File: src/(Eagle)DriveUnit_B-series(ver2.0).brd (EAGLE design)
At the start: 65.7 x 51 mm, 70 parts, among them IC1 A3921, IC2 CZ3A07, SW1 TVAF06-A020B-R, SW2 TVAF06-A020B-R, SW3 THAF01-NC-R, SW4 SS-12D00G3

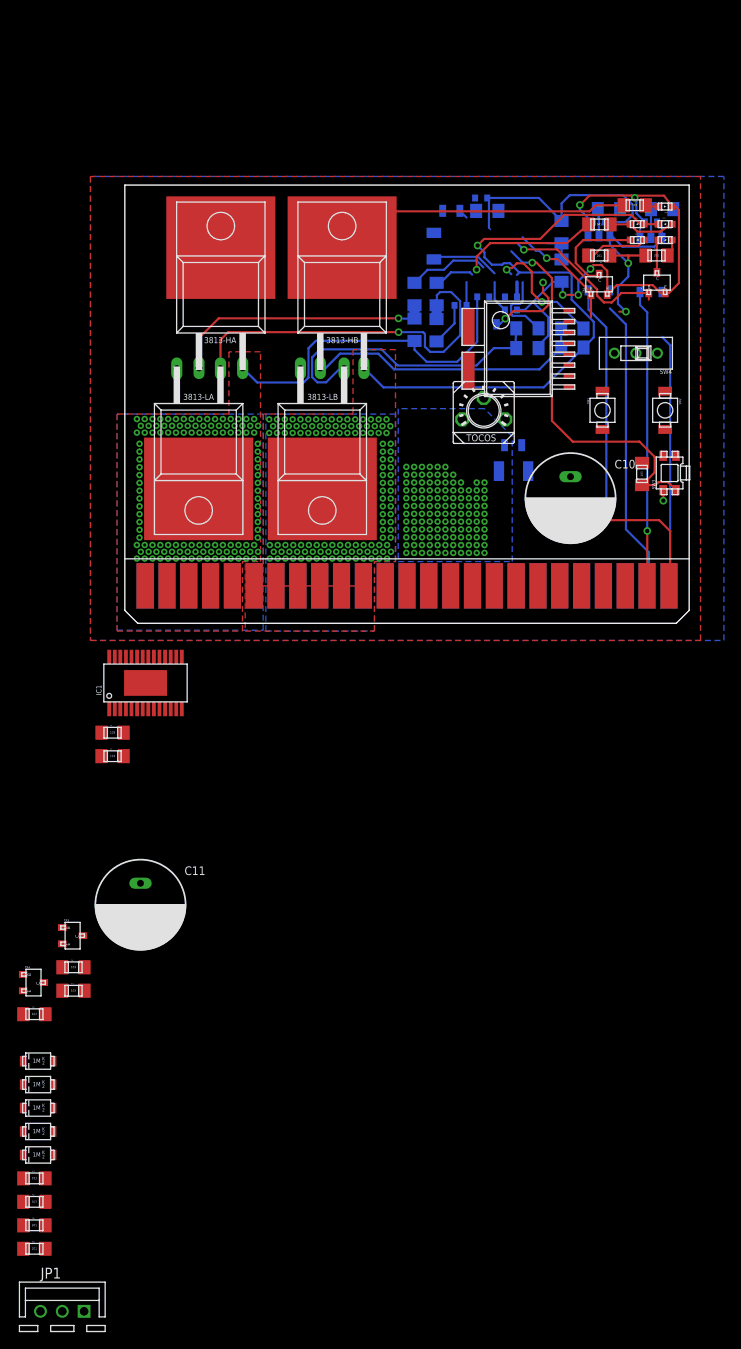
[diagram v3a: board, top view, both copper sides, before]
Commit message: [remove:電流センサを取り除いた
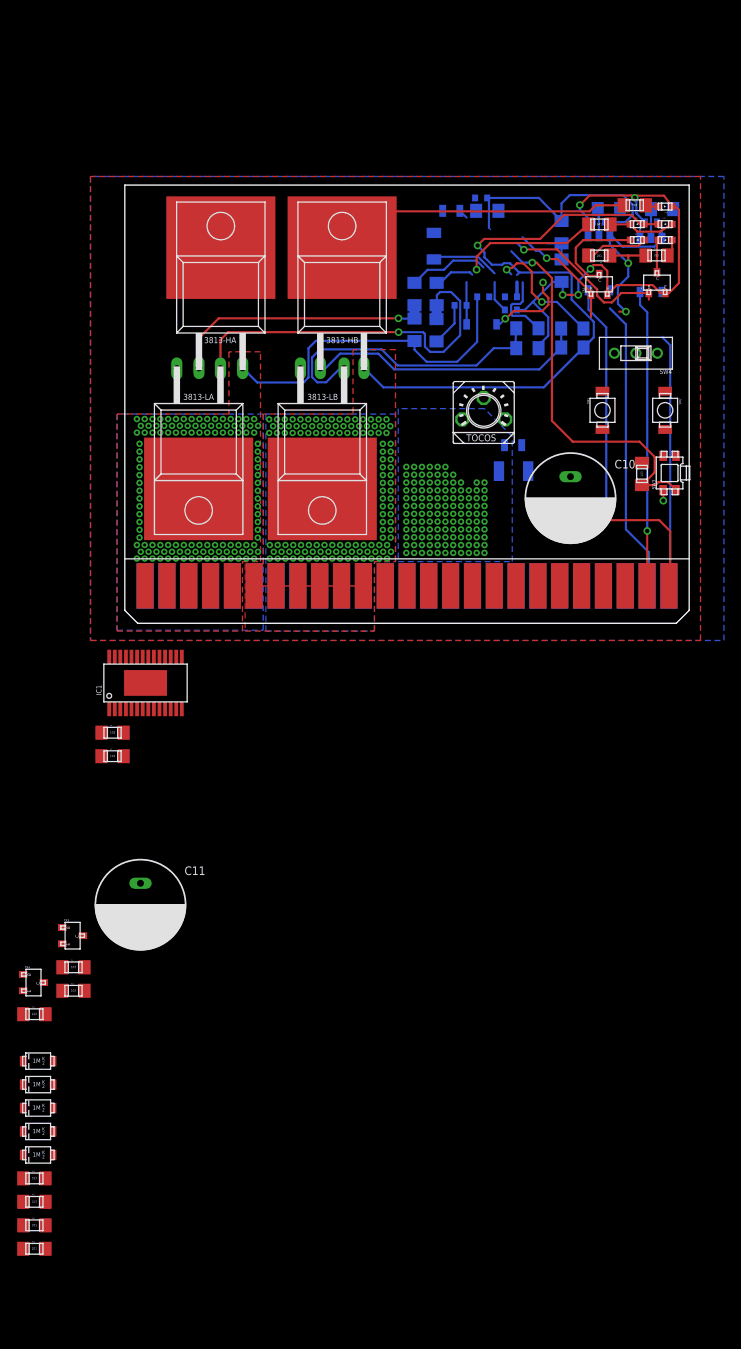
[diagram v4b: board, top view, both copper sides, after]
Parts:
- removed IC2: CZ3A07, CZ3A07:CZ3A07
- removed JP1: (no value), con-jst-xh:B3B-XH
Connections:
- removed net VOUT: JP1.2
- net GND_IN: no longer IC2.OCD2, IC2.REF2, IC2.VSS1, JP1.1
- net SA: no longer IC2.IP
- net SB: no longer IC2.IN
- net VCC_IN: no longer JP1.3
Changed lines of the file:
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@@
 </element>
 <element name="R28" library="GF063P B104K" package="GF063PB104K" value="100k" x="38.22" y="20.93" smashed="yes"/>
-<element name="IC2" library="CZ3A07" package="CZ3A07" value="CZ3A07" x="41.86" y="26.39" smashed="yes"/>
-<element name="JP1" library="con-jst-xh" package="B3B-XH" value="" x="-7.28" y="-80.08" smashed="yes">
-<attribute name="NAME" x="-9.82" y="-76.27" size="1.27" layer="25"/>
-<attribute name="VALUE" x="-9.82" y="-83.89" size="1.27" layer="27"/>
-</element>
 </elements>
 <signals>
@@
 <wire x1="45.63" y1="40.5332875" x2="45.91243125" y2="40.81571875" width="0.254" layer="16"/>
 <contactref element="IC1" pad="4"/>
-<contactref element="IC2" pad="IN"/>
 <wire x1="45.63" y1="40.5332875" x2="45.64" y2="39.71" width="0" layer="19" extent="16-16"/>
 <wire x1="27.72" y1="23.73" x2="27.83" y2="29.72" width="0" layer="19" extent="1-1"/>
@@
 <wire x1="17.6" y1="4.35" x2="17.6" y2="4.35" width="0" layer="19" extent="1-16"/>
 <wire x1="22.98" y1="15.6446" x2="23.17" y2="22.15" width="0" layer="19" extent="1-1"/>
-<wire x1="39.915" y1="29.39" x2="45.64" y2="38" width="0" layer="19" extent="1-16"/>
 <wire x1="0.13" y1="-10" x2="15.06" y2="4.35" width="0" layer="19" extent="1-1"/>
 </signal>
@@
 </polygon>
 <contactref element="IC1" pad="11"/>
-<contactref element="IC2" pad="IP"/>
 <wire x1="41.08" y1="38.07" x2="41.08" y2="41.0132" width="0" layer="19" extent="16-16"/>
-<wire x1="39.915" y1="34.49" x2="41.01" y2="38" width="0" layer="19" extent="1-16"/>
 <wire x1="13.23" y1="23.77" x2="13.71" y2="29.72" width="0" layer="19" extent="1-1"/>
 <wire x1="12.775" y1="22.98" x2="13.23" y2="23.77" width="0" layer="19" extent="1-1"/>
@@
 <wire x1="60.8" y1="4.37" x2="60.78" y2="4.35" width="0.1524" layer="1"/>
 <contactref element="TLP2" pad="3"/>
-<contactref element="JP1" pad="1"/>
-<contactref element="IC2" pad="VSS1"/>
-<contactref element="IC2" pad="REF2"/>
-<contactref element="IC2" pad="OCD2"/>
-<wire x1="51.705" y1="35.115" x2="53.91" y2="38.75" width="0" layer="19" extent="1-16"/>
-<wire x1="51.705" y1="30.035" x2="51.705" y2="35.115" width="0" layer="19" extent="1-1"/>
-<wire x1="51.705" y1="27.495" x2="51.705" y2="30.035" width="0" layer="19" extent="1-1"/>
 <wire x1="59.96" y1="38.55" x2="53.91" y2="38.75" width="0" layer="19" extent="16-16"/>
-<wire x1="-4.74" y1="-80.08" x2="60.78" y2="4.35" width="0" layer="19" extent="1-1"/>
 </signal>
 <signal name="PWM_IN">
@@
 <wire x1="58.32" y1="10.93" x2="61" y2="8.25" width="0.254" layer="16"/>
 <wire x1="61" y1="8.25" x2="61" y2="4.57" width="0.254" layer="16"/>
-<contactref element="JP1" pad="3"/>
-<wire x1="60.78" y1="4.35" x2="-9.82" y2="-80.08" width="0" layer="19" extent="16-16"/>
 </signal>
 <signal name="N$1">
@@
 <wire x1="44.27" y1="23.73" x2="41.77" y2="26.23" width="0" layer="19" extent="1-1"/>
 </signal>
-<signal name="VOUT">
-<contactref element="JP1" pad="2"/>
-</signal>
 </signals>

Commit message: [add]配線の追加
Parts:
- removed 3813-HA, 3813-HB, 3813-LA, 3813-LB: IRLB3813NOHOLE, OKUDA_libraries:TO-220AB-NOHOLE
- added HA, HB, LA, LB: IRLB3813NOHOLE, OKUDA_libraries:TO-220AB-NOHOLE
- moved R25 143.0 mm to (36.0, 67.4), flipped to the bottom
- moved R24 138.7 mm to (30.9, 67.4), flipped to the bottom
- moved D5 129.6 mm to (16.9, 69.9), flipped to the bottom
- moved D4 125.9 mm to (11.9, 69.9), flipped to the bottom
- moved R17 122.5 mm to (51.2, 64.8), flipped to the bottom
- moved R23 119.0 mm to (25.8, 67.4), flipped to the bottom
- moved D6 117.6 mm to (53.1, 39.0), turned to 90 degrees
- moved R6 117.4 mm to (52.5, 61.0), flipped to the bottom
- moved D3 115.7 mm to (55.9, 42.8), turned to 270 degrees
- moved R27 114.3 mm to (63.3, 13.4), flipped to the bottom, turned to 270 degrees
- moved R26 109.5 mm to (59.1, 13.4), flipped to the bottom, turned to 270 degrees
- moved TR4 109.1 mm to (37.3, 54.7), flipped to the bottom
- moved D2 105.3 mm to (51.4, 22.3), turned to 270 degrees
- moved TR3 100.1 mm to (32.2, 54.7), flipped to the bottom
- moved R5 83.8 mm to (61.3, 38.5)
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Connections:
- net GND: now also LA.SOURCE, LB.SOURCE; no longer 3813-LA.SOURCE, 3813-LB.SOURCE
- net N$13: now also HA.GATE; no longer 3813-HA.GATE
- net N$21: now also HB.GATE; no longer 3813-HB.GATE
- net N$25: now also LA.GATE; no longer 3813-LA.GATE
- net N$26: now also LB.GATE; no longer 3813-LB.GATE
- net SA: now also HA.SOURCE, LA.DRAIN; no longer 3813-HA.SOURCE, 3813-LA.DRAIN
- net SB: now also HB.SOURCE, LB.DRAIN; no longer 3813-HB.SOURCE, 3813-LB.DRAIN
- net VCC: now also HA.DRAIN, HB.DRAIN; no longer 3813-HA.DRAIN, 3813-HB.DRAIN
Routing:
- net SB: track 93.0 -> 0.00 mm, vias 123 -> 0
- net GND: track 72.9 -> 3.98 mm, vias 6 -> 0
- net SA: track 56.1 -> 0.00 mm, vias 123 -> 0
- net V5: track 56.9 -> 3.96 mm, vias 2 -> 0
- net VCC: track 46.2 -> 0.00 mm, vias 124 -> 0
- net RESET: track 44.7 -> 0.00 mm, vias 1 -> 0
- net N$25: track 44.3 -> 0.00 mm, vias 1 -> 0
- net PWM_IN: track 42.0 -> 0.00 mm, vias 1 -> 0
- net N$26: track 35.1 -> 0.00 mm
- net GND_IN: track 34.6 -> 0.00 mm, vias 1 -> 0
- net VCC_IN: track 34.3 -> 0.00 mm
- net N$21: track 32.8 -> 0.00 mm
- net N$13: track 31.1 -> 0.00 mm, vias 1 -> 0
- net DIR_IN: track 29.5 -> 0.00 mm
- net FF1: track 19.9 -> 0.00 mm, vias 1 -> 0
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- removed copper zone on layer 1, net SA
- removed copper zone on layer 16, net SA
- removed copper zone on layer 1, net SB
- removed copper zone on layer 16, net SB
- removed copper zone on layer 16, net VCC
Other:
- board text added: "FF1"
- board text added: "FF2"
- board text added: "POW"
- board text added: "SA"
- board text added: "SB"

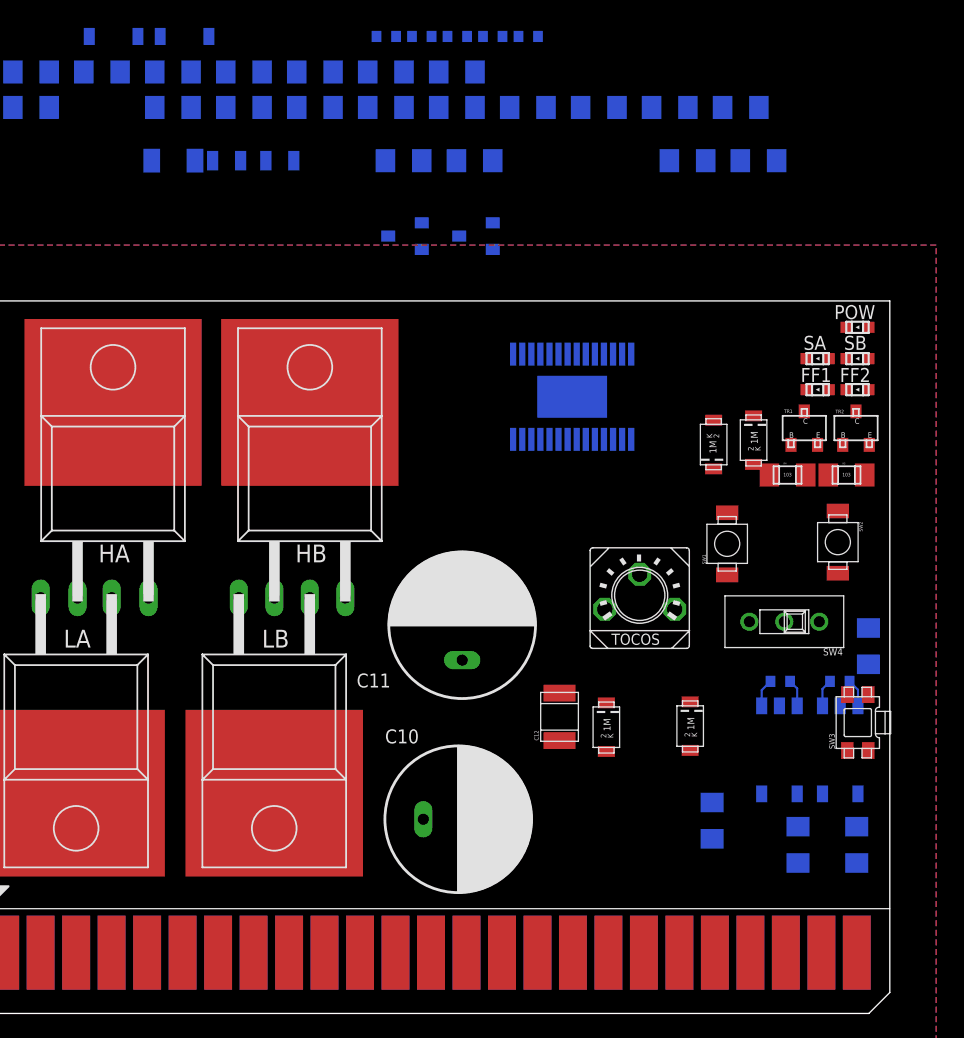
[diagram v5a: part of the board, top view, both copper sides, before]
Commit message: 入力部の配線の追加
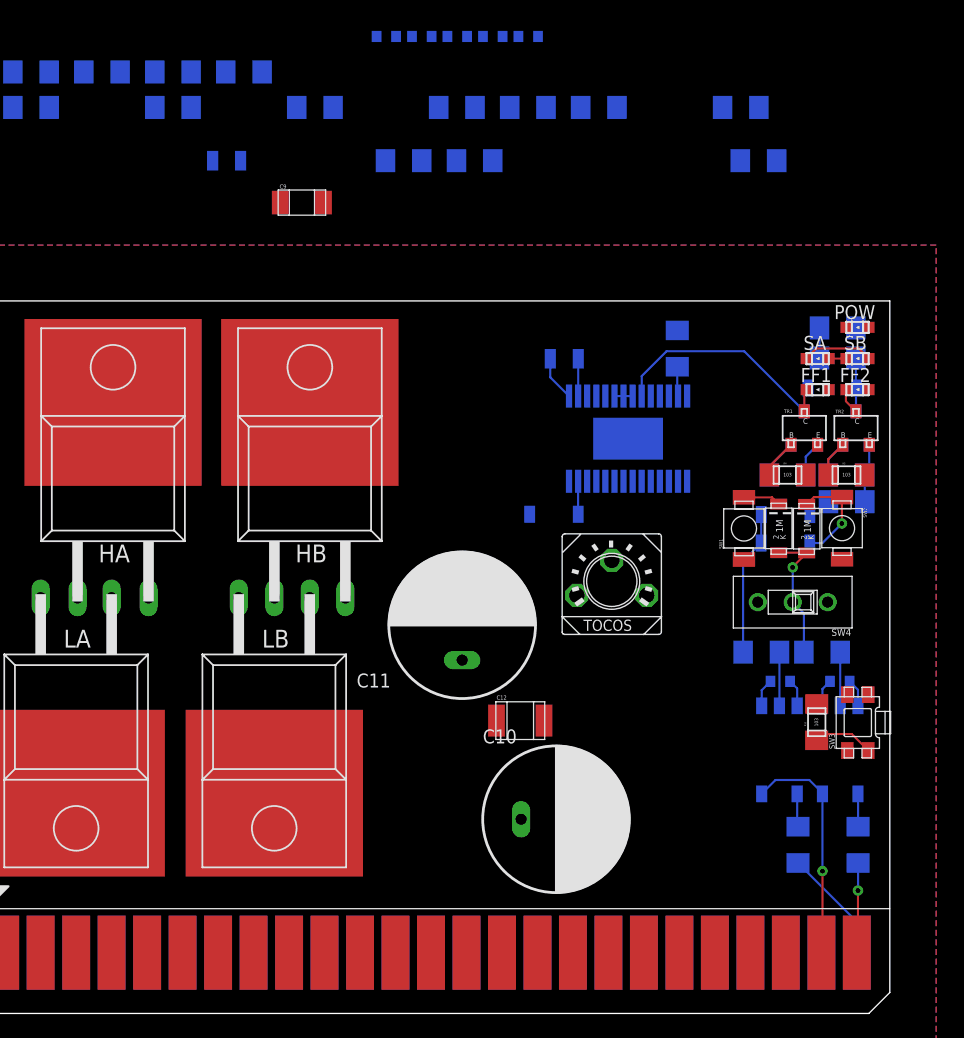
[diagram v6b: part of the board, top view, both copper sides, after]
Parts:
- moved R11 60.2 mm to (60.5, 19.6), flipped to the top, turned to 90 degrees
- moved D4 56.8 mm to (57.7, 36.5), flipped to the top, turned to 270 degrees
- moved D5 54.3 mm to (59.7, 36.4), flipped to the top, turned to 270 degrees
- moved R24 43.8 mm to (63.9, 38.5)
- moved R23 42.7 mm to (63.2, 46.9)
- moved R25 37.3 mm to (59.7, 38.5)
- moved R17 30.9 mm to (63.9, 36.6)
- moved TR3 29.9 mm to (58.6, 40.7), turned to 90 degrees
- moved TR4 28.7 mm to (62.3, 40.7), turned to 90 degrees
- moved R13 27.0 mm to (50.5, 46.3), turned to 90 degrees
- moved C6 24.8 mm to (42.4, 46.9), turned to 180 degrees
- moved D2 15.9 mm to (60.0, 35.7), flipped to the bottom, turned to 0 degrees
- moved R6 14.5 mm to (60.6, 49.1), turned to 180 degrees
- moved D1 13.6 mm to (43.4, 35.7), flipped to the bottom, turned to 0 degrees
- moved R1 11.0 mm to (55.2, 25.9), turned to 180 degrees
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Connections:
- new net N$27: D2.A, D6.A, R1.LEFT
- net DIR: no longer D2.A, D6.A, R1.LEFT
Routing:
- net GND_IN: track 0.00 -> 16.6 mm, vias 0 -> 1
- net PWM: track 0.00 -> 15.6 mm
- net LAP: track 0.00 -> 12.4 mm, vias 0 -> 1
- net N$27: track 0.00 -> 10.4 mm
- net DIR_IN: track 0.00 -> 8.16 mm
- net N$20: track 0.00 -> 7.52 mm, vias 0 -> 1
- net N$17: track 0.00 -> 6.90 mm
- net PWM_IN: track 0.00 -> 6.46 mm, vias 0 -> 1
- net GND: track 3.98 -> 9.37 mm
- net SB: track 0.00 -> 5.10 mm
- net RESET: track 0.00 -> 4.37 mm
- net N$12: track 0.00 -> 3.86 mm
- net N$14: track 0.00 -> 3.84 mm
- net N$11: track 0.00 -> 3.84 mm
- net V5: track 3.96 -> 7.41 mm
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
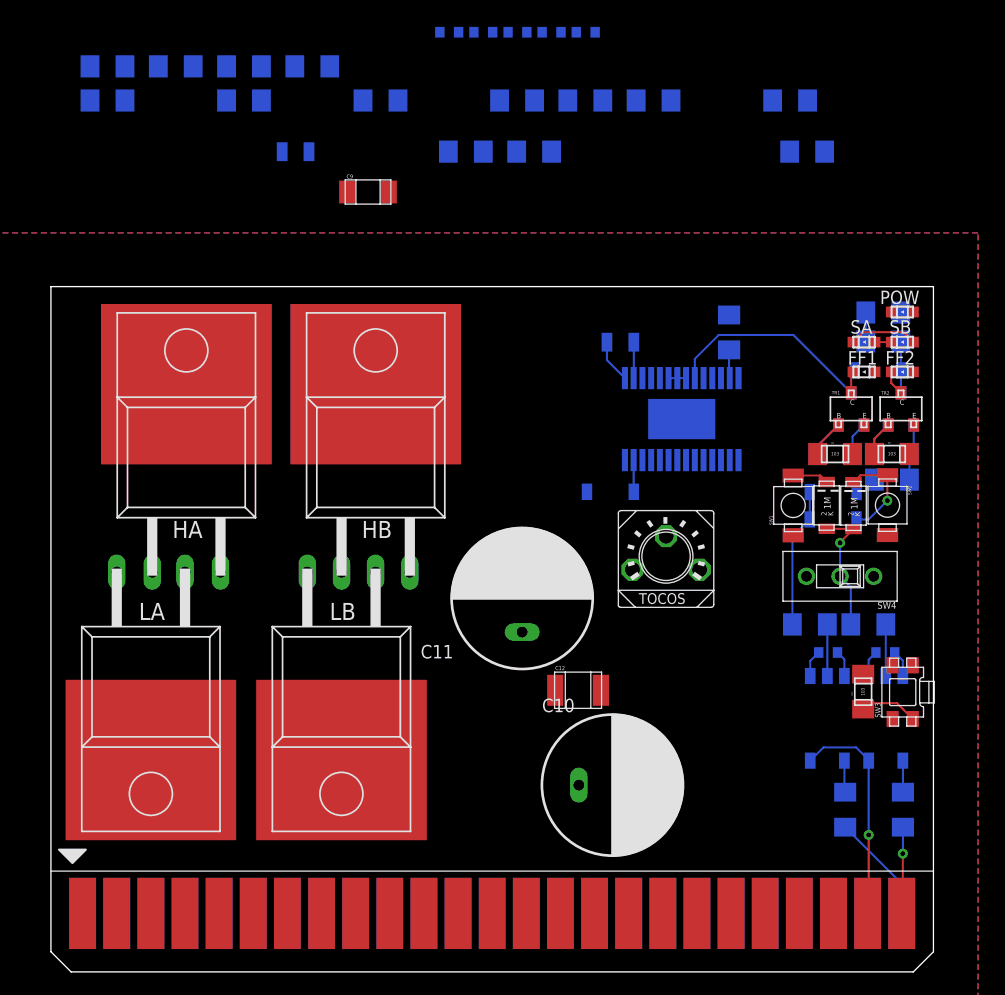
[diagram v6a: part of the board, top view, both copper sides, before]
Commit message: [add]部品配置完了
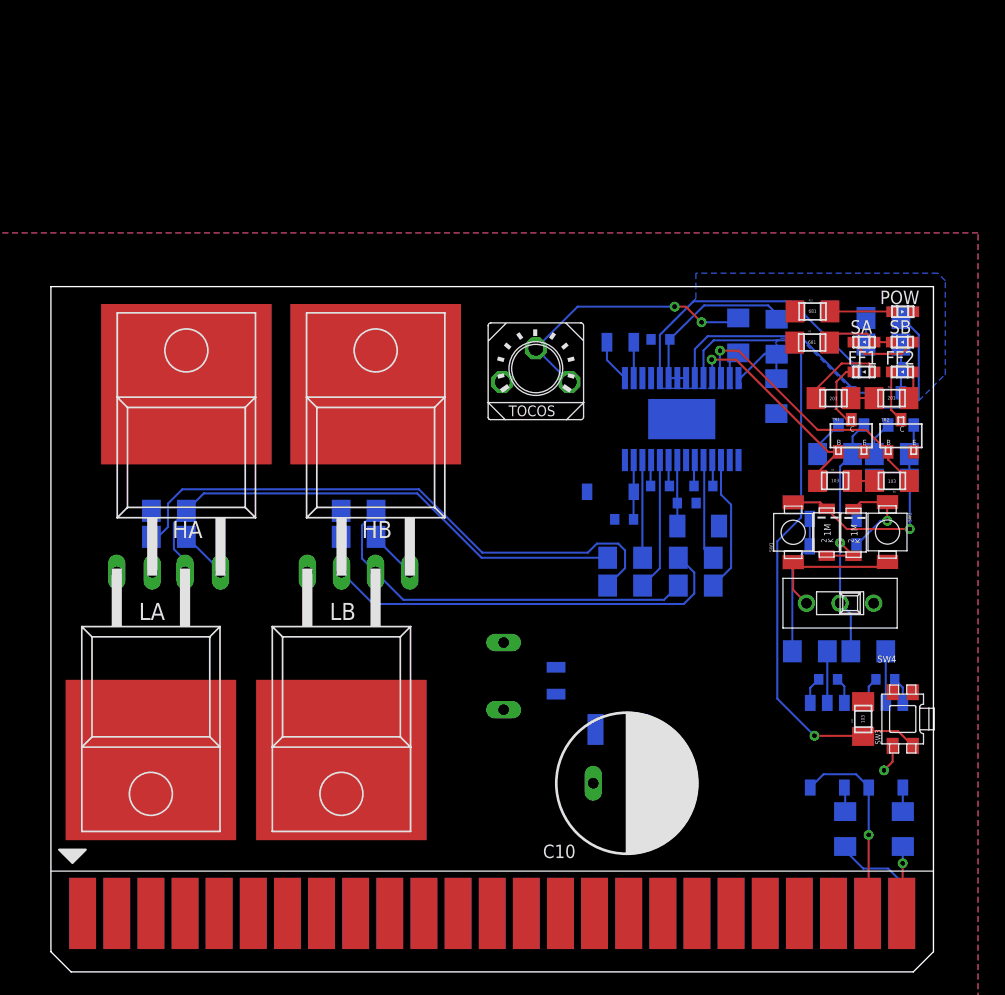
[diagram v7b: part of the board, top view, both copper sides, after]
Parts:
- moved R8 60.0 mm to (61.3, 42.7), flipped to the top
- moved R10 49.3 mm to (49.3, 28.8)
- moved R16 48.5 mm to (10.1, 32.4)
- moved R20 47.8 mm to (41.4, 30.8), turned to 180 degrees
- moved R21 46.4 mm to (41.4, 28.8), turned to 180 degrees
- moved R18 46.2 mm to (21.6, 34.3), turned to 180 degrees
- moved R15 45.4 mm to (7.48, 34.3), turned to 180 degrees
- moved C13 43.9 mm to (37.6, 21.7), turned to 90 degrees
- moved R12 41.3 mm to (49.3, 30.8)
- moved R19 39.7 mm to (24.2, 32.4)
- moved R22 39.1 mm to (55.4, 49.1), flipped to the top
- moved C4 38.2 mm to (47.3, 34.9)
- moved C5 37.1 mm to (42.7, 33.7), turned to 180 degrees
- moved C7 35.6 mm to (48.6, 36.2), turned to 180 degrees
- moved C9 35.0 mm to (48.2, 33.2), flipped to the bottom, turned to 180 degrees
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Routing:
- net RESET: track 4.37 -> 48.5 mm, vias 0 -> 1
- net N$13: track 0.00 -> 43.3 mm
- net N$25: track 0.00 -> 39.2 mm
- net N$21: track 0.00 -> 33.4 mm
- net N$26: track 0.00 -> 29.2 mm
- net DIR: track 0.00 -> 21.1 mm
- net N$16: track 0.00 -> 20.5 mm, vias 0 -> 2
- net FF2: track 2.59 -> 20.5 mm, vias 0 -> 1
- net V5: track 7.41 -> 23.1 mm
- net FF1: track 2.80 -> 16.5 mm, vias 0 -> 1
- net PWM: track 15.6 -> 28.6 mm
- net GND: track 9.37 -> 22.2 mm, vias 0 -> 1
- net N$17: track 6.90 -> 17.4 mm, vias 0 -> 1
- net GLB: track 0.00 -> 10.2 mm
- net GHA: track 0.00 -> 9.87 mm
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- added copper zone on layer 16, net V5
